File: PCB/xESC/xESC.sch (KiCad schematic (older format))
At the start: 17 parts, among them U1 ATmega328-AU, Y1 Resonator

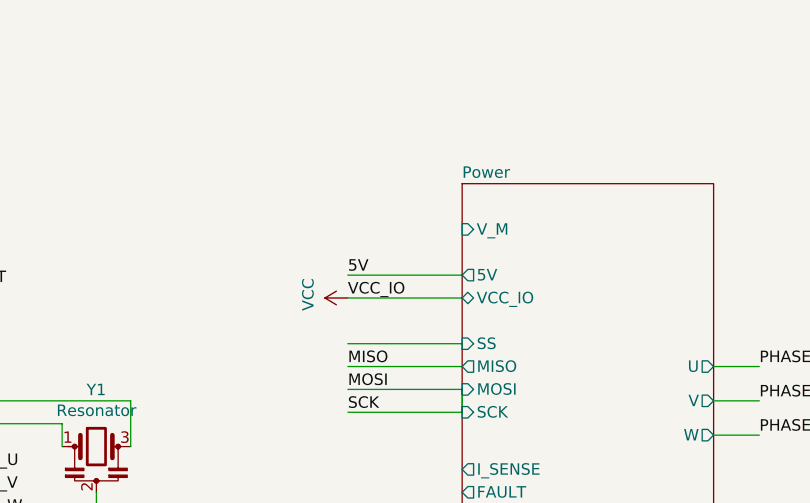
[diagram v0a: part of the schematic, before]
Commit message: added missing connection
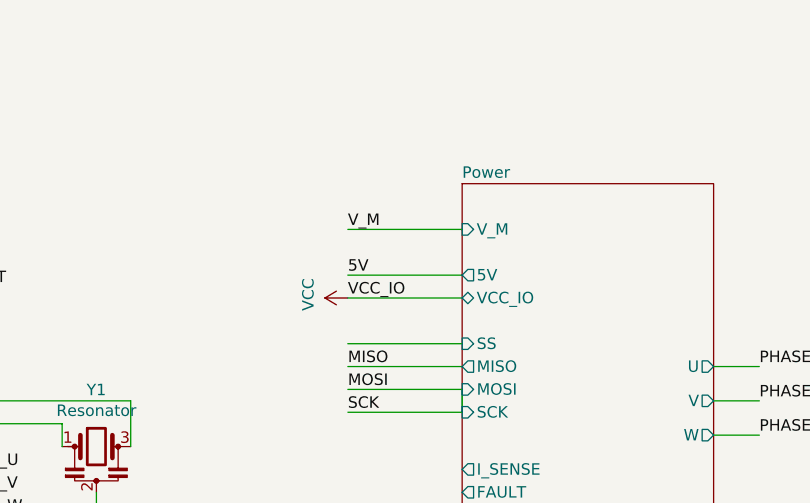
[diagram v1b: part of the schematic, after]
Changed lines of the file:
@@
 Text Label 1750 4050 0    50   ~ 0
 INPUT
+Wire Wire Line
+	9350 2250 8850 2250
+Text Label 8850 2250 0    50   ~ 0
+V_M
 $EndSCHEMATC

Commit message: wip
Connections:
- net MOSI: no longer U1.17 (PB5)
- net FAULT: now reaches U1.12 (PB0)
- net I_SENSE: now reaches U1.26 (PC3)
- net DRV_ENABLE: now reaches U1.27 (PC4)
- net DRV_SS: now reaches U1.28 (PC5)
- new net SCK: U1.17 (PB5)
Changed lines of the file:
@@
 Text Label 3900 3350 0    50   ~ 0
 HALL_W
-$Sheet
-S 9350 2050 1100 2750
-U 6183112C
-F0 "Power" 50
-F1 "Power.sch" 50
-F2 "V_M" I L 9350 2250 50
-F3 "VCC_IO" B L 9350 2550 50
-F4 "SS" I L 9350 2750 50
-F5 "SCK" I L 9350 3050 50
-F6 "ENABLE" I L 9350 3500 50
-F7 "FAULT" O L 9350 3400 50
-F8 "MOSI" I L 9350 2950 50
-F9 "MISO" O L 9350 2850 50
-F10 "I_SENSE" O L 9350 3300 50
-F11 "UH" I L 9350 3800 50
-F12 "UL" I L 9350 3900 50
-F13 "VH" I L 9350 4100 50
-F14 "VL" I L 9350 4200 50
-F15 "WH" I L 9350 4400 50
-F16 "WL" I L 9350 4500 50
-F17 "5V" O L 9350 2450 50
-F18 "U" O R 10450 2850 50
-F19 "V" O R 10450 3000 50
-F20 "W" O R 10450 3150 50
-$EndSheet
 Wire Wire Line
 	10450 2850 10650 2850
@@
 	6700 2700 7150 2700
 Wire Wire Line
-	6700 2900 7150 2900
-Wire Wire Line
 	9350 2850 8850 2850
 Wire Wire Line
-	9350 2950 9350 3050
-Wire Wire Line
-	9350 2950 8850 2950
-Wire Wire Line
-	8850 3050 9350 3050
-Wire Wire Line
 	9350 2750 8850 2750
-Text Label 7150 2700 0    50   ~ 0
-MOSI
 Text Label 7150 2800 0    50   ~ 0
 MISO
-Text Label 7150 2900 0    50   ~ 0
-SCK
-Text Label 8850 2950 0    50   ~ 0
-MOSI
 Text Label 8850 2850 0    50   ~ 0
 MISO
-Text Label 8850 3050 0    50   ~ 0
-SCK
-Text Label 1800 5000 0    50   ~ 0
-MOSI
 Text Label 1800 4900 0    50   ~ 0
 MISO
-Text Label 1800 5100 0    50   ~ 0
-SCK
 Wire Wire Line
 	6700 2500 6800 2500
@@
 Text Label 8850 2250 0    50   ~ 0
 V_M
+Wire Wire Line
+	6700 3600 7150 3600
+Wire Wire Line
+	6700 2400 7150 2400
+Text Label 7150 2400 0    50   ~ 0
+FAULT
+Text Label 8850 3400 0    50   ~ 0
+FAULT
+Text Label 8850 3500 0    50   ~ 0
+DRV_ENABLE
+Text Label 8850 3300 0    50   ~ 0
+I_SENSE
+Text Label 7150 3600 0    50   ~ 0
+I_SENSE
+Wire Wire Line
+	9350 3300 8850 3300
+Wire Wire Line
+	8850 3400 9350 3400
+Wire Wire Line
+	9350 3500 8850 3500
+Wire Wire Line
+	6700 3700 7150 3700
+Text Label 7150 3700 0    50   ~ 0
+DRV_ENABLE
+Text Label 8850 2750 0    50   ~ 0
+DRV_SS
+Text Label 7150 3800 0    50   ~ 0
+DRV_SS
+Wire Wire Line
+	7150 3800 6700 3800
+Text Label 7150 2900 0    50   ~ 0
+SCK
+Wire Wire Line
+	6700 2900 7150 2900
+Text Label 7150 2700 0    50   ~ 0
+MOSI
+Text Label 8850 3050 0    50   ~ 0
+SCK
+Text Label 1800 5100 0    50   ~ 0
+SCK
+Text Label 1800 5000 0    50   ~ 0
+MOSI
+Wire Wire Line
+	9350 2950 8850 2950
+Wire Wire Line
+	8850 3050 9350 3050
+$Sheet
+S 9350 2050 1100 2750
+U 6183112C
+F0 "Power" 50
+F1 "Power.sch" 50
+F2 "V_M" I L 9350 2250 50
+F3 "VCC_IO" B L 9350 2550 50
+F4 "SS" I L 9350 2750 50
+F5 "SCK" I L 9350 3050 50
+F6 "ENABLE" I L 9350 3500 50
+F7 "FAULT" O L 9350 3400 50
+F8 "MOSI" I L 9350 2950 50
+F9 "MISO" O L 9350 2850 50
+F10 "I_SENSE" O L 9350 3300 50
+F11 "UH" I L 9350 3800 50
+F12 "UL" I L 9350 3900 50
+F13 "VH" I L 9350 4100 50
+F14 "VL" I L 9350 4200 50
+F15 "WH" I L 9350 4400 50
+F16 "WL" I L 9350 4500 50
+F17 "5V" O L 9350 2450 50
+F18 "U" O R 10450 2850 50
+F19 "V" O R 10450 3000 50
+F20 "W" O R 10450 3150 50
+$EndSheet
+Text Label 8850 2950 0    50   ~ 0
+MOSI
 $EndSCHEMATC

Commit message: wip
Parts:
- C14: footprint (none) -> Capacitor_SMD:C_0805_2012Metric_Pad1.18x1.45mm_HandSolder
- C15, C16, C17, C18, C19: renamed from C?; footprint (none) -> Capacitor_SMD:C_0805_2012Metric_Pad1.18x1.45mm_HandSolder
- gave numbers to parts that had none: 8
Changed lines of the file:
@@
 F 0 "C14" H 4815 2846 50  0000 L CNN
 F 1 "100nF" H 4815 2755 50  0000 L CNN
-F 2 "" H 4738 2650 50  0001 C CNN
+F 2 "Capacitor_SMD:C_0805_2012Metric_Pad1.18x1.45mm_HandSolder" H 4738 2650 50  0001 C CNN
 F 3 "~" H 4700 2800 50  0001 C CNN
 	1    4700 2800
@@
 P 5300 4150
 AR Path="/6183112C/61829070" Ref="C?"  Part="1"
-AR Path="/61829070" Ref="C?"  Part="1"
-F 0 "C?" H 5415 4196 50  0000 L CNN
+AR Path="/61829070" Ref="C19"  Part="1"
+F 0 "C19" H 5415 4196 50  0000 L CNN
 F 1 "100nF" H 5415 4105 50  0000 L CNN
-F 2 "" H 5338 4000 50  0001 C CNN
+F 2 "Capacitor_SMD:C_0805_2012Metric_Pad1.18x1.45mm_HandSolder" H 5338 4000 50  0001 C CNN
 F 3 "~" H 5300 4150 50  0001 C CNN
 	1    5300 4150
@@
 P 5000 4150
 AR Path="/6183112C/61829B27" Ref="C?"  Part="1"
-AR Path="/61829B27" Ref="C?"  Part="1"
-F 0 "C?" H 5115 4196 50  0000 L CNN
+AR Path="/61829B27" Ref="C18"  Part="1"
+F 0 "C18" H 5115 4196 50  0000 L CNN
 F 1 "100nF" H 5115 4105 50  0000 L CNN
-F 2 "" H 5038 4000 50  0001 C CNN
+F 2 "Capacitor_SMD:C_0805_2012Metric_Pad1.18x1.45mm_HandSolder" H 5038 4000 50  0001 C CNN
 F 3 "~" H 5000 4150 50  0001 C CNN
 	1    5000 4150
@@
 	5150 3800 5300 3800
 $Comp
-L power:GND #PWR?
+L power:GND #PWR0111
 U 1 1 6182BA1C
 P 5150 4700
-F 0 "#PWR?" H 5150 4450 50  0001 C CNN
+F 0 "#PWR0111" H 5150 4450 50  0001 C CNN
 F 1 "GND" H 5155 4527 50  0000 C CNN
 F 2 "" H 5150 4700 50  0001 C CNN
@@
 $EndComp
 $Comp
-L power:VCC #PWR?
+L power:VCC #PWR0112
 U 1 1 6182C830
 P 5150 3650
-F 0 "#PWR?" H 5150 3500 50  0001 C CNN
+F 0 "#PWR0112" H 5150 3500 50  0001 C CNN
 F 1 "VCC" H 5165 3823 50  0000 C CNN
 F 2 "" H 5150 3650 50  0001 C CNN
@@
 Place close to pins 3+4, 5+6
 $Comp
-L Device:R R?
+L Device:R R15
 U 1 1 61834C4B
 P 6900 2050
-F 0 "R?" H 6970 2096 50  0000 L CNN
+F 0 "R15" H 6970 2096 50  0000 L CNN
 F 1 "10kR" H 6970 2005 50  0000 L CNN
 F 2 "Resistor_SMD:R_0805_2012Metric" V 6830 2050 50  0001 C CNN
@@
 P 2400 3650
 AR Path="/6183112C/61860011" Ref="C?"  Part="1"
-AR Path="/61860011" Ref="C?"  Part="1"
-F 0 "C?" H 2515 3696 50  0000 L CNN
+AR Path="/61860011" Ref="C15"  Part="1"
+F 0 "C15" H 2515 3696 50  0000 L CNN
 F 1 "10pF" H 2515 3605 50  0000 L CNN
-F 2 "" H 2438 3500 50  0001 C CNN
+F 2 "Capacitor_SMD:C_0805_2012Metric_Pad1.18x1.45mm_HandSolder" H 2438 3500 50  0001 C CNN
 F 3 "~" H 2400 3650 50  0001 C CNN
 	1    2400 3650
@@
 P 2650 3650
 AR Path="/6183112C/6186137B" Ref="C?"  Part="1"
-AR Path="/6186137B" Ref="C?"  Part="1"
-F 0 "C?" H 2765 3696 50  0000 L CNN
+AR Path="/6186137B" Ref="C16"  Part="1"
+F 0 "C16" H 2765 3696 50  0000 L CNN
 F 1 "10pF" H 2765 3605 50  0000 L CNN
-F 2 "" H 2688 3500 50  0001 C CNN
+F 2 "Capacitor_SMD:C_0805_2012Metric_Pad1.18x1.45mm_HandSolder" H 2688 3500 50  0001 C CNN
 F 3 "~" H 2650 3650 50  0001 C CNN
 	1    2650 3650
@@
 P 2900 3650
 AR Path="/6183112C/618625E4" Ref="C?"  Part="1"
-AR Path="/618625E4" Ref="C?"  Part="1"
-F 0 "C?" H 3015 3696 50  0000 L CNN
+AR Path="/618625E4" Ref="C17"  Part="1"
+F 0 "C17" H 3015 3696 50  0000 L CNN
 F 1 "10pF" H 3015 3605 50  0000 L CNN
-F 2 "" H 2938 3500 50  0001 C CNN
+F 2 "Capacitor_SMD:C_0805_2012Metric_Pad1.18x1.45mm_HandSolder" H 2938 3500 50  0001 C CNN
 F 3 "~" H 2900 3650 50  0001 C CNN
 	1    2900 3650
@@
 	1400 3150 2900 3150
 $Comp
-L Device:R R?
+L Device:R R12
 U 1 1 6186ABCD
 P 2400 2800
-F 0 "R?" H 2470 2846 50  0000 L CNN
+F 0 "R12" H 2470 2846 50  0000 L CNN
 F 1 "1kR" H 2470 2755 50  0000 L CNN
 F 2 "Resistor_SMD:R_0805_2012Metric" V 2330 2800 50  0001 C CNN
@@
 $EndComp
 $Comp
-L Device:R R?
+L Device:R R13
 U 1 1 6186DD06
 P 2650 2800
-F 0 "R?" H 2720 2846 50  0000 L CNN
+F 0 "R13" H 2720 2846 50  0000 L CNN
 F 1 "1kR" H 2720 2755 50  0000 L CNN
 F 2 "Resistor_SMD:R_0805_2012Metric" V 2580 2800 50  0001 C CNN
@@
 $EndComp
 $Comp
-L Device:R R?
+L Device:R R14
 U 1 1 6186F2CF
 P 2900 2800
-F 0 "R?" H 2970 2846 50  0000 L CNN
+F 0 "R14" H 2970 2846 50  0000 L CNN
 F 1 "1kR" H 2970 2755 50  0000 L CNN
 F 2 "Resistor_SMD:R_0805_2012Metric" V 2830 2800 50  0001 C CNN
@@
 	2650 4050 2900 4050
 $Comp
-L power:GND #PWR?
+L power:GND #PWR0113
 U 1 1 6187926B
 P 2650 4100
-F 0 "#PWR?" H 2650 3850 50  0001 C CNN
+F 0 "#PWR0113" H 2650 3850 50  0001 C CNN
 F 1 "GND" H 2655 3927 50  0000 C CNN
 F 2 "" H 2650 4100 50  0001 C CNN
@@
 	2650 2450 2900 2450
 $Comp
-L Jumper:SolderJumper_3_Bridged12 JP?
+L Jumper:SolderJumper_3_Bridged12 JP9
 U 1 1 618804A4
 P 2650 2150
-F 0 "JP?" H 2650 2355 50  0000 C CNN
+F 0 "JP9" H 2650 2355 50  0000 C CNN
 F 1 "SolderJumper_3_Bridged12" H 2650 2264 50  0000 C CNN
 F 2 "Jumper:SolderJumper-3_P1.3mm_Bridged12_Pad1.0x1.5mm_NumberLabels" H 2650 2150 50  0001 C CNN
@@
 	2400 3350 3300 3350
 $Comp
-L Device:D_Schottky D?
+L Device:D_Schottky D2
 U 1 1 618AA33D
 P 3300 2750
-F 0 "D?" V 3254 2830 50  0000 L CNN
+F 0 "D2" V 3254 2830 50  0000 L CNN
 F 1 "D_Schottky" V 3345 2830 50  0000 L CNN
 F 2 "Diode_SMD:D_0805_2012Metric_Pad1.15x1.40mm_HandSolder" H 3300 2750 50  0001 C CNN
@@
 $EndComp
 $Comp
-L Device:D_Schottky D?
+L Device:D_Schottky D3
 U 1 1 618AB2E8
 P 3500 2750
-F 0 "D?" V 3454 2830 50  0000 L CNN
+F 0 "D3" V 3454 2830 50  0000 L CNN
 F 1 "D_Schottky" V 3545 2830 50  0000 L CNN
 F 2 "Diode_SMD:D_0805_2012Metric_Pad1.15x1.40mm_HandSolder" H 3500 2750 50  0001 C CNN
@@
 $EndComp
 $Comp
-L Device:D_Schottky D?
+L Device:D_Schottky D4
 U 1 1 618AD730
 P 3700 2750
-F 0 "D?" V 3654 2830 50  0000 L CNN
+F 0 "D4" V 3654 2830 50  0000 L CNN
 F 1 "D_Schottky" V 3745 2830 50  0000 L CNN
 F 2 "Diode_SMD:D_0805_2012Metric_Pad1.15x1.40mm_HandSolder" H 3700 2750 50  0001 C CNN
@@
 	3700 3150 3900 3150
 $Comp
-L power:VCC #PWR?
+L power:VCC #PWR0114
 U 1 1 618B76AE
 P 3500 2000
-F 0 "#PWR?" H 3500 1850 50  0001 C CNN
+F 0 "#PWR0114" H 3500 1850 50  0001 C CNN
 F 1 "VCC" H 3515 2173 50  0000 C CNN
 F 2 "" H 3500 2000 50  0001 C CNN
@@
 	3700 2450 3500 2450
 $Comp
-L power:VCC #PWR?
+L power:VCC #PWR0115
 U 1 1 618C424A
 P 8850 2550
-F 0 "#PWR?" H 8850 2400 50  0001 C CNN
+F 0 "#PWR0115" H 8850 2400 50  0001 C CNN
 F 1 "VCC" H 8865 2723 50  0000 C CNN
 F 2 "" H 8850 2550 50  0001 C CNN
@@
 	1900 2650 1900 2750
 $Comp
-L power:GND #PWR?
+L power:GND #PWR0116
 U 1 1 6190BFEA
 P 1900 2750
-F 0 "#PWR?" H 1900 2500 50  0001 C CNN
+F 0 "#PWR0116" H 1900 2500 50  0001 C CNN
 F 1 "GND" H 1905 2577 50  0000 C CNN
 F 2 "" H 1900 2750 50  0001 C CNN

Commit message: wip
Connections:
- net INPUT renamed INPUT_ANALOG
- net INPUT_ANALOG: no longer U1.13 (PB1)
- new net INPUT_PWM: U1.13 (PB1)
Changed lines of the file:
@@
 F8 "TXD" I R 1400 3700 50
 F9 "RXD" O R 1400 3800 50
-F10 "INPUT" O R 1400 4050 50
-F11 "U" I R 1400 4200 50
-F12 "V" I R 1400 4300 50
-F13 "W" I R 1400 4400 50
-F14 "VCCIO" I R 1400 2450 50
-F15 "RESET" I R 1400 4800 50
-F16 "MISO" I R 1400 4900 50
-F17 "MOSI" I R 1400 5000 50
-F18 "SCK" I R 1400 5100 50
+F10 "U" I R 1400 4200 50
+F11 "V" I R 1400 4300 50
+F12 "W" I R 1400 4400 50
+F13 "VCCIO" I R 1400 2450 50
+F14 "RESET" I R 1400 4800 50
+F15 "MISO" I R 1400 4900 50
+F16 "MOSI" I R 1400 5000 50
+F17 "SCK" I R 1400 5100 50
+F18 "INPUT_PWM" O R 1400 3950 50
+F19 "INPUT_ANALOG" O R 1400 4050 50
 $EndSheet
 $Comp
@@
 Text Label 1800 4900 0    50   ~ 0
 MISO
-Wire Wire Line
-	6700 2500 6800 2500
 Text Label 7150 2500 0    50   ~ 0
-INPUT
+INPUT_PWM
 Wire Wire Line
 	1400 4050 1750 4050
-Wire Wire Line
-	6800 2500 6800 2000
-Wire Wire Line
-	6800 2000 5350 2000
-Wire Wire Line
-	5350 2000 5350 2600
-Wire Wire Line
-	5350 2600 5500 2600
-Connection ~ 6800 2500
-Wire Wire Line
-	6800 2500 7150 2500
 Text Label 1750 4050 0    50   ~ 0
-INPUT
+INPUT_ANALOG
 Wire Wire Line
 	9350 2250 8850 2250
@@
 Text Label 8850 2950 0    50   ~ 0
 MOSI
+Wire Wire Line
+	1400 3950 1750 3950
+Text Label 1750 3950 0    50   ~ 0
+INPUT_PWM
+Wire Wire Line
+	6700 2500 7150 2500
+Text Label 4850 2600 0    50   ~ 0
+INPUT_ANALOG
+Wire Wire Line
+	4850 2600 5500 2600
 $EndSCHEMATC

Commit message: wip
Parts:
- removed D2, D3, D4: D_Schottky, Diode_SMD:D_0805_2012Metric_Pad1.15x1.40mm_HandSolder, symbol Device:D_Schottky
- removed JP8: SolderJumper_2_Open, Jumper:SolderJumper-2_P1.3mm_Open_Pad1.0x1.5mm, symbol Jumper:SolderJumper_2_Open
- removed JP9: SolderJumper_3_Bridged12, Jumper:SolderJumper-3_P1.3mm_Bridged12_Pad1.0x1.5mm_NumberLabels, symbol Jumper:SolderJumper_3_Bridged12
- added H1, H2, H3, H4: MountingHole_Pad, MountingHole:MountingHole_2.2mm_M2_Pad, symbol Mechanical:MountingHole_Pad
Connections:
- net GND: now also H1.1, H2.1, H3.1, H4.1
- net VCC: now also R12.1, R13.1, R14.1
- net EXT_SPI_SS: now reaches U1.14 (PB2)
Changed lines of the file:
@@
 F2 "V_IN" O R 1400 2550 50
 F3 "GND" U R 1400 2650 50
-F4 "HALL_V+" I R 1400 3050 50
-F5 "HALL_U" O R 1400 3150 50
-F6 "HALL_V" O R 1400 3250 50
-F7 "HALL_W" O R 1400 3350 50
-F8 "TXD" I R 1400 3700 50
-F9 "RXD" O R 1400 3800 50
-F10 "U" I R 1400 4200 50
-F11 "V" I R 1400 4300 50
-F12 "W" I R 1400 4400 50
-F13 "VCCIO" I R 1400 2450 50
-F14 "RESET" I R 1400 4800 50
-F15 "MISO" I R 1400 4900 50
-F16 "MOSI" I R 1400 5000 50
-F17 "SCK" I R 1400 5100 50
-F18 "INPUT_PWM" O R 1400 3950 50
-F19 "INPUT_ANALOG" O R 1400 4050 50
+F4 "HALL_U" O R 1400 3150 50
+F5 "HALL_V" O R 1400 3250 50
+F6 "HALL_W" O R 1400 3350 50
+F7 "TXD" I R 1400 3700 50
+F8 "RXD" O R 1400 3800 50
+F9 "U" I R 1400 4200 50
+F10 "V" I R 1400 4300 50
+F11 "W" I R 1400 4400 50
+F12 "VCCIO" I R 1400 2450 50
+F13 "RESET" I R 1400 4800 50
+F14 "MISO" I R 1400 4900 50
+F15 "MOSI" I R 1400 5000 50
+F16 "SCK" I R 1400 5100 50
+F17 "INPUT_PWM" O R 1400 3950 50
+F18 "INPUT_ANALOG" O R 1400 4050 50
 $EndSheet
 $Comp
@@
 	6200 1750 6100 1750
 Connection ~ 6100 1750
-Wire Wire Line
-	6100 1750 6100 1650
 $Comp
 L MCU_Microchip_ATmega:ATmega328-AU U1
@@
 Wire Wire Line
 	1400 2450 1900 2450
-Wire Wire Line
-	1900 2450 1900 2150
 $Comp
 L power:VCC #PWR0103
@@
 Wire Wire Line
 	6100 5350 6100 5100
-Wire Wire Line
-	4700 2400 4700 2050
-Connection ~ 4700 2400
-$Comp
-L Jumper:SolderJumper_2_Open JP8
-U 1 1 6181EAAC
-P 4700 1900
-F 0 "JP8" V 4654 1968 50  0000 L CNN
-F 1 "SolderJumper_2_Open" V 4745 1968 50  0000 L CNN
-F 2 "Jumper:SolderJumper-2_P1.3mm_Open_Pad1.0x1.5mm" H 4700 1900 50  0001 C CNN
-F 3 "~" H 4700 1900 50  0001 C CNN
-	1    4700 1900
-	0    1    1    0
-$EndComp
-Wire Wire Line
-	4700 1750 4700 1650
-Wire Wire Line
-	4700 1650 6100 1650
-Connection ~ 6100 1650
-Wire Wire Line
-	6100 1650 6100 1550
 $Comp
 L Device:Resonator Y1
@@
 W_DIR
 Wire Wire Line
-	8850 2450 9350 2450
-Wire Wire Line
 	9350 2550 8850 2550
 Text Label 8850 2550 0    50   ~ 0
 VCC_IO
-Text Label 8850 2450 0    50   ~ 0
-5V
-Wire Wire Line
-	1400 3050 1800 3050
-Text Label 1800 3050 0    50   ~ 0
-5V
 $Comp
 L Device:C C?
@@
 Wire Wire Line
 	2650 2450 2900 2450
-$Comp
-L Jumper:SolderJumper_3_Bridged12 JP9
-U 1 1 618804A4
-P 2650 2150
-F 0 "JP9" H 2650 2355 50  0000 C CNN
-F 1 "SolderJumper_3_Bridged12" H 2650 2264 50  0000 C CNN
-F 2 "Jumper:SolderJumper-3_P1.3mm_Bridged12_Pad1.0x1.5mm_NumberLabels" H 2650 2150 50  0001 C CNN
-F 3 "~" H 2650 2150 50  0001 C CNN
-	1    2650 2150
-	1    0    0    -1
-$EndComp
-Wire Wire Line
-	2650 2450 2650 2300
-Wire Wire Line
-	1900 2150 2450 2150
-Connection ~ 1900 2150
-Wire Wire Line
-	1900 2150 1900 2000
-Wire Wire Line
-	2850 2150 3200 2150
-Text Label 3200 2150 0    50   ~ 0
-5V
-Wire Wire Line
-	2900 3150 3700 3150
-Wire Wire Line
-	2650 3250 3500 3250
-Wire Wire Line
-	2400 3350 3300 3350
-$Comp
-L Device:D_Schottky D2
-U 1 1 618AA33D
-P 3300 2750
-F 0 "D2" V 3254 2830 50  0000 L CNN
-F 1 "D_Schottky" V 3345 2830 50  0000 L CNN
-F 2 "Diode_SMD:D_0805_2012Metric_Pad1.15x1.40mm_HandSolder" H 3300 2750 50  0001 C CNN
-F 3 "~" H 3300 2750 50  0001 C CNN
-	1    3300 2750
-	0    1    1    0
-$EndComp
-$Comp
-L Device:D_Schottky D3
-U 1 1 618AB2E8
-P 3500 2750
-F 0 "D3" V 3454 2830 50  0000 L CNN
-F 1 "D_Schottky" V 3545 2830 50  0000 L CNN
-F 2 "Diode_SMD:D_0805_2012Metric_Pad1.15x1.40mm_HandSolder" H 3500 2750 50  0001 C CNN
-F 3 "~" H 3500 2750 50  0001 C CNN
-	1    3500 2750
-	0    1    1    0
-$EndComp
-$Comp
-L Device:D_Schottky D4
-U 1 1 618AD730
-P 3700 2750
-F 0 "D4" V 3654 2830 50  0000 L CNN
-F 1 "D_Schottky" V 3745 2830 50  0000 L CNN
-F 2 "Diode_SMD:D_0805_2012Metric_Pad1.15x1.40mm_HandSolder" H 3700 2750 50  0001 C CNN
-F 3 "~" H 3700 2750 50  0001 C CNN
-	1    3700 2750
-	0    1    1    0
-$EndComp
-Wire Wire Line
-	3300 3350 3300 2900
-Connection ~ 3300 3350
-Wire Wire Line
-	3300 3350 3900 3350
-Wire Wire Line
-	3500 3250 3500 2900
-Connection ~ 3500 3250
-Wire Wire Line
-	3500 3250 3900 3250
-Wire Wire Line
-	3700 3150 3700 2900
-Connection ~ 3700 3150
-Wire Wire Line
-	3700 3150 3900 3150
-$Comp
-L power:VCC #PWR0114
-U 1 1 618B76AE
-P 3500 2000
-F 0 "#PWR0114" H 3500 1850 50  0001 C CNN
-F 1 "VCC" H 3515 2173 50  0000 C CNN
-F 2 "" H 3500 2000 50  0001 C CNN
-F 3 "" H 3500 2000 50  0001 C CNN
-	1    3500 2000
-	1    0    0    -1
-$EndComp
-Wire Wire Line
-	3300 2600 3300 2450
-Wire Wire Line
-	3300 2450 3500 2450
-Wire Wire Line
-	3500 2450 3500 2000
-Wire Wire Line
-	3500 2600 3500 2450
-Connection ~ 3500 2450
-Wire Wire Line
-	3700 2600 3700 2450
-Wire Wire Line
-	3700 2450 3500 2450
 $Comp
 L power:VCC #PWR0115
@@
 F15 "WH" I L 9350 4400 50
 F16 "WL" I L 9350 4500 50
-F17 "5V" O L 9350 2450 50
-F18 "U" O R 10450 2850 50
-F19 "V" O R 10450 3000 50
-F20 "W" O R 10450 3150 50
+F17 "U" O R 10450 2850 50
+F18 "V" O R 10450 3000 50
+F19 "W" O R 10450 3150 50
 $EndSheet
 Text Label 8850 2950 0    50   ~ 0
@@
 Wire Wire Line
 	4850 2600 5500 2600
+Wire Wire Line
+	6100 1550 6100 1750
+$Comp
+L Mechanical:MountingHole_Pad H1
+U 1 1 61C71604
+P 2650 6400
+F 0 "H1" H 2750 6449 50  0000 L CNN
+F 1 "MountingHole_Pad" H 2750 6358 50  0000 L CNN
+F 2 "MountingHole:MountingHole_2.2mm_M2_Pad" H 2650 6400 50  0001 C CNN
+F 3 "~" H 2650 6400 50  0001 C CNN
+	1    2650 6400
+	1    0    0    -1
+$EndComp
+Wire Wire Line
+	2650 6500 2650 6700
+Wire Wire Line
+	2650 6700 2850 6700
+Wire Wire Line
+	3250 6700 3250 6500
+Wire Wire Line
+	3050 6500 3050 6700
+Connection ~ 3050 6700
+Wire Wire Line
+	3050 6700 3250 6700
+Wire Wire Line
+	2850 6700 2850 6500
+Connection ~ 2850 6700
+Wire Wire Line
+	2850 6700 2950 6700
+$Comp
+L power:GND #PWR0119
+U 1 1 61C8FEAA
+P 2950 6700
+F 0 "#PWR0119" H 2950 6450 50  0001 C CNN
+F 1 "GND" H 2955 6527 50  0000 C CNN
+F 2 "" H 2950 6700 50  0001 C CNN
+F 3 "" H 2950 6700 50  0001 C CNN
+	1    2950 6700
+	1    0    0    -1
+$EndComp
+Connection ~ 2950 6700
+Wire Wire Line
+	2950 6700 3050 6700
+$Comp
+L Mechanical:MountingHole_Pad H2
+U 1 1 61C9B6F5
+P 2850 6400
+F 0 "H2" H 2950 6449 50  0000 L CNN
+F 1 "MountingHole_Pad" H 2950 6358 50  0000 L CNN
+F 2 "MountingHole:MountingHole_2.2mm_M2_Pad" H 2850 6400 50  0001 C CNN
+F 3 "~" H 2850 6400 50  0001 C CNN
+	1    2850 6400
+	1    0    0    -1
+$EndComp
+$Comp
+L Mechanical:MountingHole_Pad H3
+U 1 1 61CA0CC2
+P 3050 6400
+F 0 "H3" H 3150 6449 50  0000 L CNN
+F 1 "MountingHole_Pad" H 3150 6358 50  0000 L CNN
+F 2 "MountingHole:MountingHole_2.2mm_M2_Pad" H 3050 6400 50  0001 C CNN
+F 3 "~" H 3050 6400 50  0001 C CNN
+	1    3050 6400
+	1    0    0    -1
+$EndComp
+$Comp
+L Mechanical:MountingHole_Pad H4
+U 1 1 61CA62C7
+P 3250 6400
+F 0 "H4" H 3350 6449 50  0000 L CNN
+F 1 "MountingHole_Pad" H 3350 6358 50  0000 L CNN
+F 2 "MountingHole:MountingHole_2.2mm_M2_Pad" H 3250 6400 50  0001 C CNN
+F 3 "~" H 3250 6400 50  0001 C CNN
+	1    3250 6400
+	1    0    0    -1
+$EndComp
+Wire Wire Line
+	1900 2000 1900 2450
+Wire Wire Line
+	2400 3350 3900 3350
+Wire Wire Line
+	2650 3250 3900 3250
+Wire Wire Line
+	2900 3150 3900 3150
+$Comp
+L power:VCC #PWR0107
+U 1 1 61CFD9F9
+P 2650 2000
+F 0 "#PWR0107" H 2650 1850 50  0001 C CNN
+F 1 "VCC" H 2665 2173 50  0000 C CNN
+F 2 "" H 2650 2000 50  0001 C CNN
+F 3 "" H 2650 2000 50  0001 C CNN
+	1    2650 2000
+	1    0    0    -1
+$EndComp
+Wire Wire Line
+	2650 2000 2650 2450
+Wire Wire Line
+	6700 2600 7150 2600
+Text Label 7150 2600 0    50   ~ 0
+EXT_SPI_SS
 $EndSCHEMATC

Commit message: added logo, version and github link
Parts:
- H1, H2, H3, H4: footprint MountingHole:MountingHole_2.2mm_M2_Pad -> MountingHole:MountingHole_2.2mm_M2_DIN965_Pad
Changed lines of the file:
@@
 F17 "INPUT_PWM" O R 1400 3950 50
 F18 "INPUT_ANALOG" O R 1400 4050 50
+F19 "SS_EXT_SPI" I R 1400 4650 50
 $EndSheet
 $Comp
@@
 F 0 "H1" H 2750 6449 50  0000 L CNN
 F 1 "MountingHole_Pad" H 2750 6358 50  0000 L CNN
-F 2 "MountingHole:MountingHole_2.2mm_M2_Pad" H 2650 6400 50  0001 C CNN
+F 2 "MountingHole:MountingHole_2.2mm_M2_DIN965_Pad" H 2650 6400 50  0001 C CNN
 F 3 "~" H 2650 6400 50  0001 C CNN
 	1    2650 6400
@@
 F 0 "H2" H 2950 6449 50  0000 L CNN
 F 1 "MountingHole_Pad" H 2950 6358 50  0000 L CNN
-F 2 "MountingHole:MountingHole_2.2mm_M2_Pad" H 2850 6400 50  0001 C CNN
+F 2 "MountingHole:MountingHole_2.2mm_M2_DIN965_Pad" H 2850 6400 50  0001 C CNN
 F 3 "~" H 2850 6400 50  0001 C CNN
 	1    2850 6400
@@
 F 0 "H3" H 3150 6449 50  0000 L CNN
 F 1 "MountingHole_Pad" H 3150 6358 50  0000 L CNN
-F 2 "MountingHole:MountingHole_2.2mm_M2_Pad" H 3050 6400 50  0001 C CNN
+F 2 "MountingHole:MountingHole_2.2mm_M2_DIN965_Pad" H 3050 6400 50  0001 C CNN
 F 3 "~" H 3050 6400 50  0001 C CNN
 	1    3050 6400
@@
 F 0 "H4" H 3350 6449 50  0000 L CNN
 F 1 "MountingHole_Pad" H 3350 6358 50  0000 L CNN
-F 2 "MountingHole:MountingHole_2.2mm_M2_Pad" H 3250 6400 50  0001 C CNN
+F 2 "MountingHole:MountingHole_2.2mm_M2_DIN965_Pad" H 3250 6400 50  0001 C CNN
 F 3 "~" H 3250 6400 50  0001 C CNN
 	1    3250 6400
@@
 Text Label 7150 2600 0    50   ~ 0
 EXT_SPI_SS
+Wire Wire Line
+	1400 4650 1850 4650
+Text Label 1850 4650 0    50   ~ 0
+EXT_SPI_SS
 $EndSCHEMATC
